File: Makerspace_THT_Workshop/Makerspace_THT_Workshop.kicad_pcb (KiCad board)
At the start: 2 copper layers, 135.6 x 104.2 mm, 24 parts, among them SW1 SW_SPDT, U1 LM358, U2 LMC555xN

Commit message: Updated the board to fix alot of stuff
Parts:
- removed D2: LED, LED_THT:LED_D5.0mm_5.0mm_Pitch
- removed the G*** at (131.8, 113.5)
- removed the G*** at (147.6, 132.4)
- removed R10: 100, Resistor_THT:R_Axial_DIN0207_L6.3mm_D2.5mm_P7.62mm_Horizontal
- added G***: LOGO, Makerspace_Decals:Makerspace_Logo_20_MASKmm, B.Cu at (100.0, 75.9)
- added G***: LOGO, Makerspace_Decals:Makerspace, B.Cu at (106.2, 69.2)
- AE1: footprint Connector_PinHeader_1.00mm:PinHeader_1x01_P1.00mm_Vertical -> TestPoint:TestPoint_Pad_D4.0mm
- BT1: footprint Battery:BatteryHolder_Keystone_3001_1x12mm -> Custom_Batteries:BK-913_MPD; moved to B.Cu
- D1: footprint LED_THT:LED_D5.0mm_5.0mm_Pitch -> LED_THT:LED_D5.0mm; moved to F.Cu
- R1, R2, R3, R4, R5, R6, R7, R8, R9: footprint Resistor_THT:R_Axial_DIN0207_L6.3mm_D2.5mm_P7.62mm_Horizontal -> Resistor_THT:R_Axial_DIN0207_L6.3mm_D2.5mm_P10.16mm_Horizontal
- RV1: footprint Potentiometer_THT:Potentiometer_ACP_CA9-V10_Vertical -> Custom_Potentiometer:601030_AVX
- SW1: moved to B.Cu
- U1: value LM358 -> Op-Amp
- moved SW1 45.5 mm to (117.9, 96.1), turned to 110 degrees
- moved R1 36.1 mm to (168.8, 118.0), turned to 135 degrees
- moved C2 24.2 mm to (147.8, 97.5), turned to -45 degrees
- moved R2 22.9 mm to (154.0, 118.8), turned to -45 degrees
- moved C1 22.2 mm to (154.8, 103.6), turned to -45 degrees
- moved BT1 20.0 mm to (131.4, 112.2), turned to 135 degrees
- moved RV1 19.3 mm to (172.2, 121.3), turned to -135 degrees
- moved R9 18.4 mm to (123.2, 88.6), turned to -45 degrees
- moved R7 17.9 mm to (133.4, 98.6), turned to -45 degrees
- moved R6 15.6 mm to (137.0, 94.4), turned to -45 degrees
- moved R4 14.9 mm to (150.8, 115.8), turned to 135 degrees
- moved R3 13.4 mm to (157.6, 115.0), turned to -45 degrees
- moved R5 11.2 mm to (154.4, 111.8), turned to 135 degrees
- moved U1 11.0 mm to (156.6, 128.2), turned to -135 degrees
- moved C3 10.6 mm to (141.0, 90.9), turned to -45 degrees
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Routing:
- net Net-(C1-Pad1): track 25.0 -> 53.8 mm
- net Net-(U1B--): track 7.74 -> 32.0 mm
- net Net-(U1B-+): track 16.8 -> 40.7 mm
- net Net-(D1-A): track 18.8 -> 39.1 mm
- net Net-(AE1-A): track 46.1 -> 62.1 mm
- net Net-(D2-A): track 15.6 -> 0.00 mm
- net Net-(BZ1-+): track 19.6 -> 33.6 mm
- net Net-(U2-DIS): track 16.6 -> 29.0 mm
- net Net-(U1A--): track 8.66 -> 17.4 mm
- net Net-(R3-Pad2): track 15.6 -> 7.96 mm
- net Net-(BT1-+): track 36.4 -> 39.3 mm
- net Net-(C1-Pad2): track 9.39 -> 11.8 mm
- net +3V0: track 84.0 -> 85.7 mm
- net Net-(U2-TR): track 66.6 -> 68.0 mm
- net GND: vias 9 -> 0
- added copper zone on F.Cu, net GND
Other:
- board size 135.6 x 104.2 mm -> 123.3 x 94.8 mm
- board text added: "AC Dino Voltage Detector V2.0"
- board text added: "Designed By: Austin Nguyen"
- board text added: "Off"
- board text added: "On"
- board text added: "Sensitivity"
- board text removed: "*Only works on alternating sources"
- board text removed: "Designed by: Austin Nguyen"
- board text removed: "Dino Sniffer Voltage Detecting Dino V1.0"

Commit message: New Version of the PCB layout
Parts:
- D1: footprint LED_THT:LED_D5.0mm -> LED_THT:LED_D5.0mm_5.0mm_Pitch
- U1: value Op-Amp -> LM358
- moved D1 3.64 mm to (116.9, 62.9), turned to -90 degrees
- moved AE1 2.50 mm to (197.1, 122.7)
- moved C3 1.08 mm to (141.9, 91.6)
- moved BT1 0.89 mm to (132.2, 112.7)
- moved C2 0.54 mm to (148.2, 97.9)
- moved C1 0.50 mm to (154.5, 104.0)
- moved R2 0.42 mm to (154.3, 118.5)
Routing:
- net Net-(AE1-A): track 62.1 -> 59.6 mm
- net Net-(D1-A): track 39.1 -> 37.9 mm
- net Net-(U2-DIS): track 29.0 -> 30.2 mm
- net Net-(C1-Pad1): track 53.8 -> 53.0 mm
- net Net-(U1A--): track 17.4 -> 18.2 mm

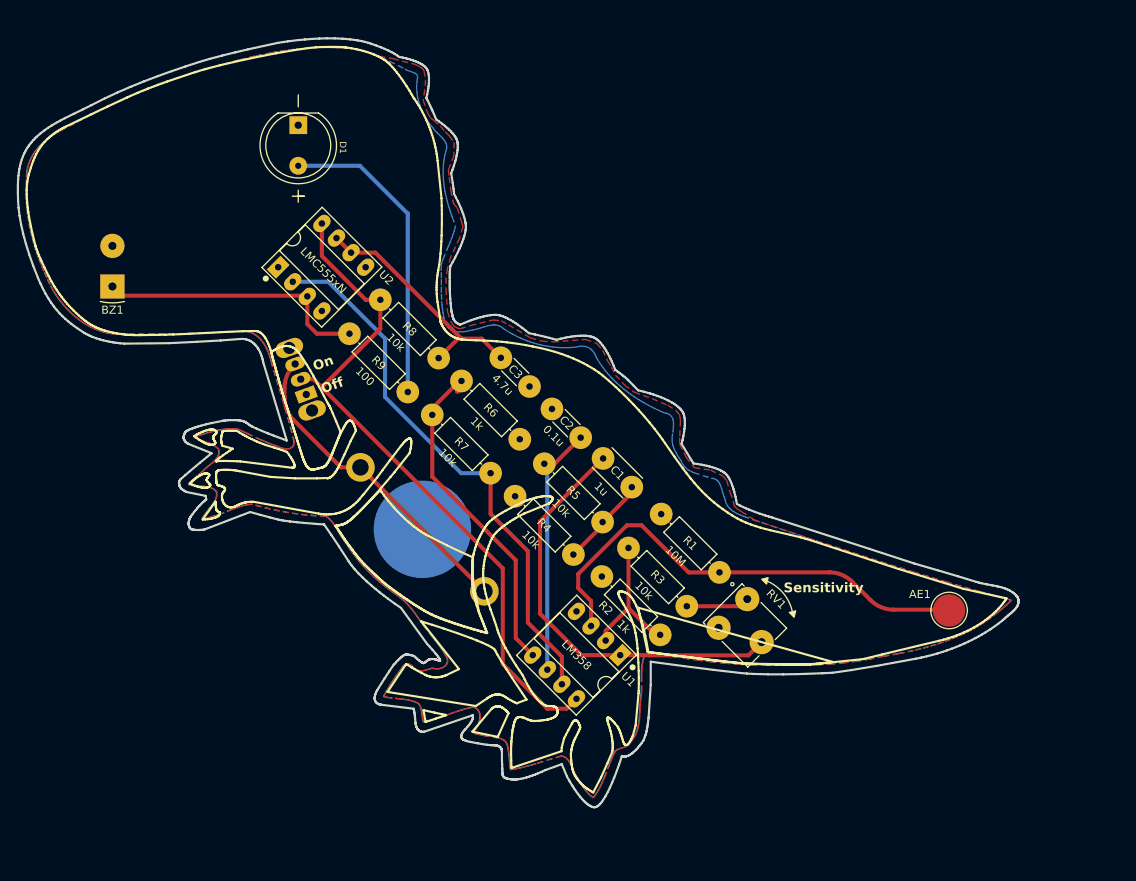
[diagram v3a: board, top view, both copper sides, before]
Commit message: Updated PCB layout, vectors, and updated references
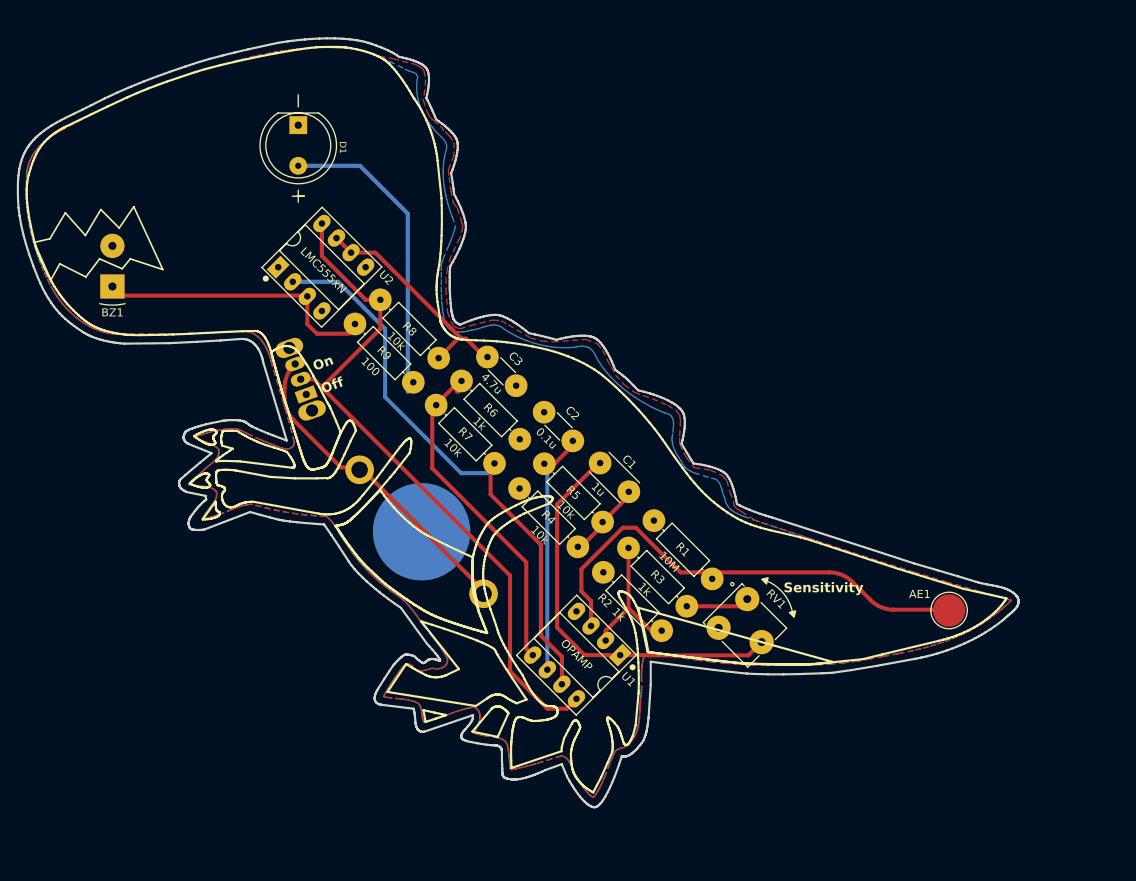
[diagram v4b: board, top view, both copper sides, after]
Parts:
- R3: value 10k -> 1k
- U1: value LM358 -> OPAMP
- moved C3 1.65 mm to (140.2, 91.5)
- moved R9 1.38 mm to (123.9, 87.4)
- moved R7 1.29 mm to (133.9, 97.4)
- moved R1 1.20 mm to (167.9, 118.8)
- moved R4 1.10 mm to (151.4, 114.9)
- moved C2 1.05 mm to (147.2, 98.3)
- moved C1 0.67 mm to (154.1, 104.5)
- moved R2 0.55 mm to (154.5, 118.0)
- moved BT1 0.32 mm to (132.1, 113.0)
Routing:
- net Net-(C1-Pad1): track 53.0 -> 51.0 mm
- net Net-(U2-DIS): track 30.2 -> 28.2 mm
- net Net-(U2-TR): track 68.0 -> 68.7 mm
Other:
- board text added: "AC Dino Voltage Detector V2.1"
- board text added: "Back Side"
- board text removed: "AC Dino Voltage Detector V2.0"
